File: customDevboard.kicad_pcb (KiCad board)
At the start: 4 copper layers, 87.7 x 87.7 mm, 245 parts, among them J10 Debug, J11 To FC, J12 TimePulse, J13 DRDY, J14 C+, J15 C-, J17 From BEC, J18 ESC Logic Power, J19 Flight Controller Power, J2 USB_C_Receptacle_USB2.0_14P, J20 From BEC, J3 From BEC, J4 From Battery, J5 U_FL-R-SMT-1_10_, J6 Debug, J7 To GPS, J8 BZ+, J9 COL, Q1 BC817, Q10 FDMS8350LET40, Q11 FDMS8350LET40, Q14 FDMS8350LET40, Q15 FDMS8350LET40, Q16 FDMS8350LET40, Q17 FDMS8350LET40, Q18 FDMS8350LET40, Q19 FDMS8350LET40, Q2 AO3401A, Q20 FDMS8350LET40, Q27 FDMS8350LET40, Q28 FDMS8350LET40, Q29 FDMS8350LET40, Q30 FDMS8350LET40, Q31 FDMS8350LET40, Q32 FDMS8350LET40, Q39 FDMS8350LET40, Q4 FDMS8350LET40, Q40 FDMS8350LET40, Q41 FDMS8350LET40, Q42 FDMS8350LET40, Q43 FDMS8350LET40, Q44 FDMS8350LET40, Q6 FDMS8350LET40, Q7 FDMS8350LET40, U1 DPS310, U10 INA181, U11 NEO-M8N, U12 TLV75733PDBV, U13 LIS3MDL, U14 FD6288Q, U15 FD6288Q, U16 FD6288Q, U17 STM32F303C8T6, U3 TPD2EUSB30, U4 TPS5430DDA, U5 STM32F722RET6, U6 TLV75733PDRV, U7 BMI270, U8 TLV75733PDBV, U9 FD6288Q, Y1 8MHz, Y2 32.768KHz, Y3 8 MHz

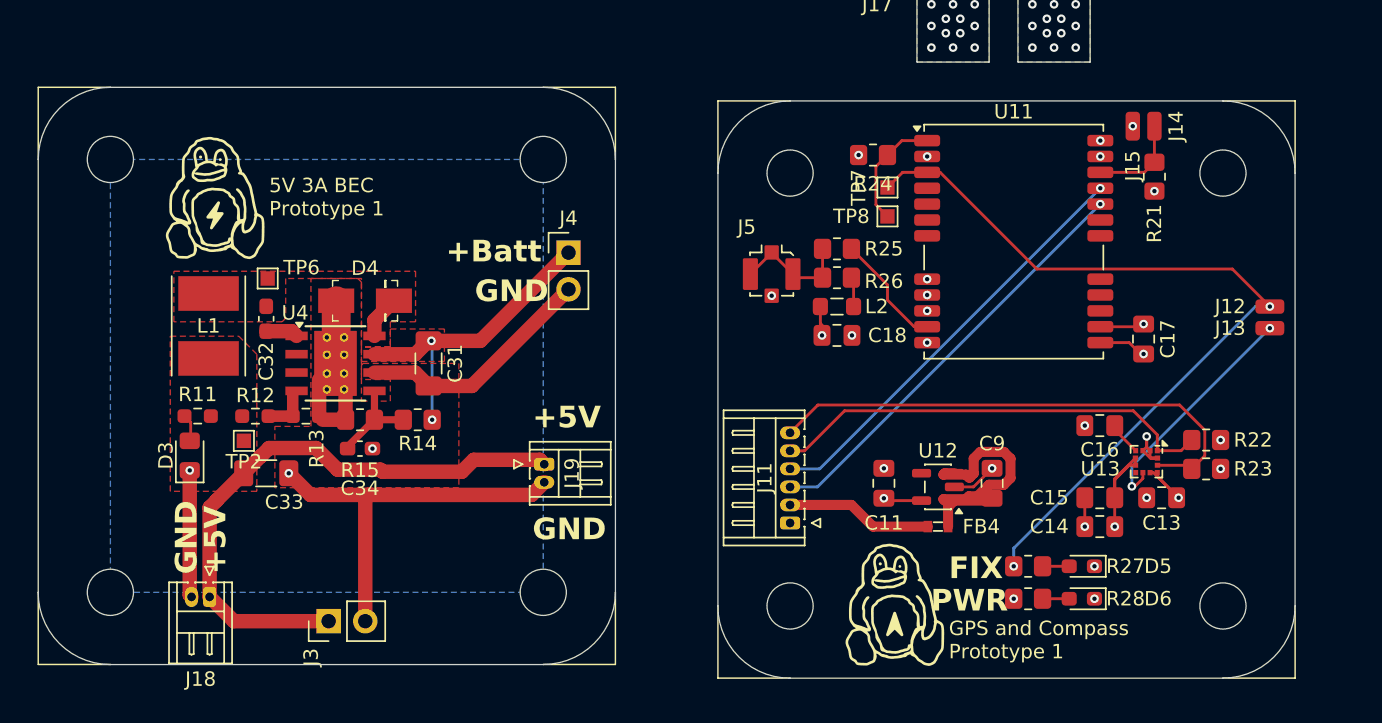
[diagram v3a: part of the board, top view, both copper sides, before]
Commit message: GPS has been moved to its own project
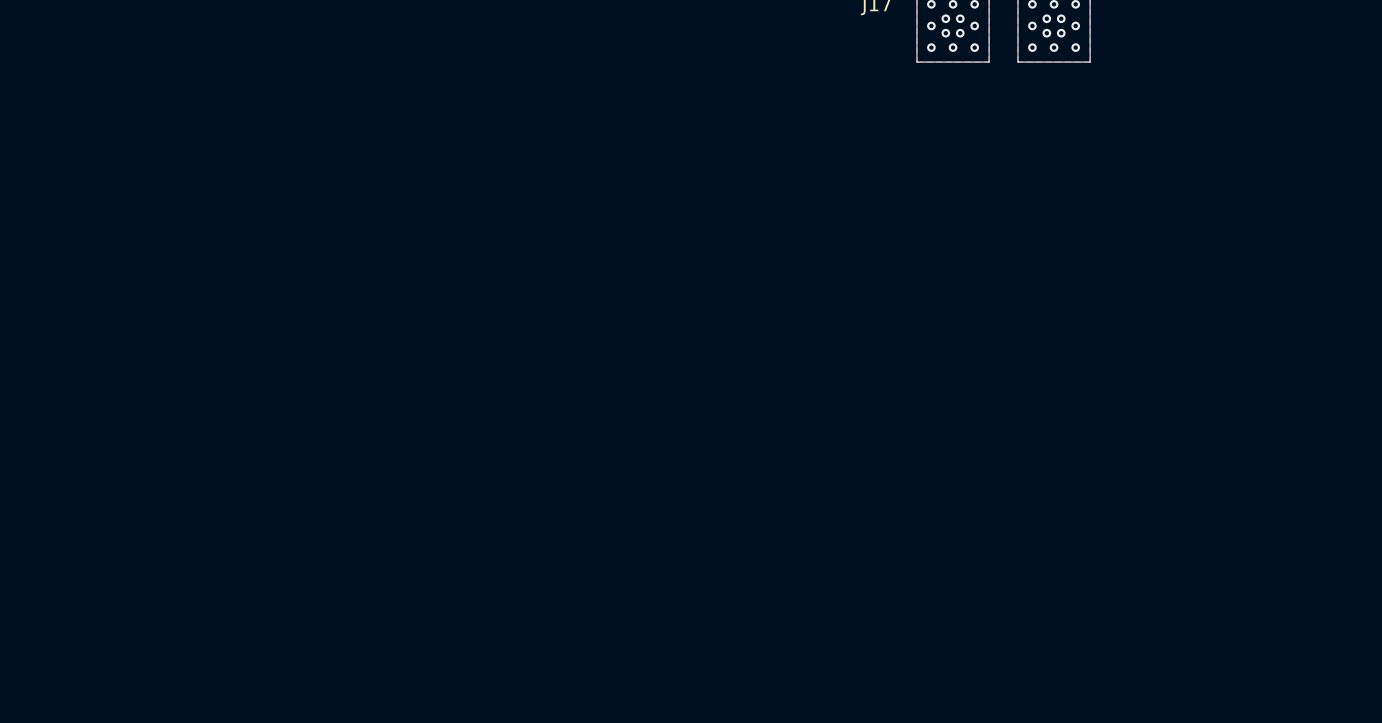
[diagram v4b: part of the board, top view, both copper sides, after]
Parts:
- removed C11, C14, C9: 1uF, Capacitor_SMD:C_0805_2012Metric_Pad1.18x1.45mm_HandSolder
- removed C13, C15, C17, C18: 100nF, Capacitor_SMD:C_0805_2012Metric_Pad1.18x1.45mm_HandSolder
- removed C16: 10nF, Capacitor_SMD:C_0805_2012Metric_Pad1.18x1.45mm_HandSolder
- removed C31: 10uF, Capacitor_SMD:C_1206_3216Metric_Pad1.33x1.80mm_HandSolder
- removed C32, C34: 10nF, Capacitor_SMD:C_0603_1608Metric_Pad1.08x0.95mm_HandSolder
- removed C33: 220uF, Capacitor_SMD:C_1206_3216Metric_Pad1.33x1.80mm_HandSolder
- removed D3: 5V LED, LED_SMD:LED_0805_2012Metric_Pad1.15x1.40mm_HandSolder
- removed D4: B340A, digikey-footprints:DO-214AC
- removed D5, D6: Status LED, LED_SMD:LED_0603_1608Metric_Pad1.05x0.95mm_HandSolder
- removed FB4: BLM18AG601SN1D, digikey-footprints:0603
- removed the G*** at (75.0, 98.2)
- removed the G*** at (27.9, 70.0)
- removed J11: To FC, Connector_Hirose:Hirose_DF13-06P-1.25DS_1x06_P1.25mm_Horizontal
- removed J12: TimePulse, Connector_Wire:SolderWirePad_1x01_SMD_1x2mm
- removed J13: DRDY, Connector_Wire:SolderWirePad_1x01_SMD_1x2mm
- removed J14: C+, Connector_Wire:SolderWirePad_1x01_SMD_1x2mm
- removed J15: C-, Connector_Wire:SolderWirePad_1x01_SMD_1x2mm
- removed J18: ESC Logic Power, Connector_Hirose:Hirose_DF13-02P-1.25DS_1x02_P1.25mm_Horizontal
- removed J19: Flight Controller Power, Connector_Hirose:Hirose_DF13-02P-1.25DS_1x02_P1.25mm_Horizontal
- removed J3: From BEC, Connector_PinHeader_2.54mm:PinHeader_1x02_P2.54mm_Vertical
- removed J4: From Battery, Connector_PinHeader_2.54mm:PinHeader_1x02_P2.54mm_Vertical
- removed J5: U_FL-R-SMT-1_10_, Connector_Coaxial:U.FL_Molex_MCRF_73412-0110_Vertical
- removed L1: 18uH, Inductor_SMD:L_Taiyo-Yuden_NR-50xx_HandSoldering
- removed L2: 10nH, Inductor_SMD:L_0805_2012Metric_Pad1.05x1.20mm_HandSolder
- removed R11: 10K, Resistor_SMD:R_0603_1608Metric_Pad0.98x0.95mm_HandSolder
- removed R12: 10k, Resistor_SMD:R_0603_1608Metric_Pad0.98x0.95mm_HandSolder
- removed R13: 3.24k, Resistor_SMD:R_0603_1608Metric_Pad0.98x0.95mm_HandSolder
- removed R14: 100k, Resistor_SMD:R_0805_2012Metric_Pad1.20x1.40mm_HandSolder
- removed R15: 18k, Resistor_SMD:R_0805_2012Metric_Pad1.20x1.40mm_HandSolder
- removed R21: 100, Resistor_SMD:R_0805_2012Metric_Pad1.20x1.40mm_HandSolder
- removed R22, R23: 47, Resistor_SMD:R_0805_2012Metric_Pad1.20x1.40mm_HandSolder
- removed R24: 10k, Resistor_SMD:R_0805_2012Metric_Pad1.20x1.40mm_HandSolder
- removed R25, R26: 0, Resistor_SMD:R_0805_2012Metric_Pad1.20x1.40mm_HandSolder
- removed R27, R28: 1K, Resistor_SMD:R_0805_2012Metric_Pad1.20x1.40mm_HandSolder
- removed the REF** at (98.0, 67.9)
- removed the REF** at (68.0, 97.9)
- removed the REF** at (20.9, 97.0)
- removed the REF** at (50.9, 67.0)
- removed the REF** at (68.0, 67.9)
- removed the REF** at (98.0, 97.9)
- removed the REF** at (20.9, 67.0)
- removed the REF** at (50.9, 97.0)
- removed TP2: +5V, TestPoint:TestPoint_Pad_1.0x1.0mm
- removed TP6: Per datasheet, TestPoint:TestPoint_Pad_1.0x1.0mm
- removed TP7: TimePulse, TestPoint:TestPoint_Pad_1.0x1.0mm
- removed TP8: SAFEBOOT, TestPoint:TestPoint_Pad_1.0x1.0mm
- removed U11: NEO-M8N, RF_GPS:ublox_NEO
- removed U12: TLV75733PDBV, Package_TO_SOT_SMD:SOT-23-5
- removed U13: LIS3MDL, Package_LGA:LGA-12_2x2mm_P0.5mm
- removed U4: TPS5430DDA, Package_SO:TI_SO-PowerPAD-8_ThermalVias
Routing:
- net BEC_GND: track 67.5 -> 0.00 mm, vias 3 -> 0
- net TimePulse: track 56.7 -> 0.00 mm, vias 2 -> 0
- net BEC_OUT: track 41.2 -> 0.00 mm
- net GPS_SDA: track 35.8 -> 0.00 mm
- net GPS_SCL: track 31.1 -> 0.00 mm
- net GPS_TX: track 29.6 -> 0.00 mm, vias 1 -> 0
- net GPS_RX: track 29.6 -> 0.00 mm, vias 1 -> 0
- net BEC_VIN: track 21.9 -> 0.00 mm, vias 2 -> 0
- net GPS_3.3V: track 21.8 -> 0.00 mm, vias 13 -> 0
- net Net-(U12-EN): track 19.1 -> 0.00 mm
- net DRDY: track 16.3 -> 0.00 mm, vias 2 -> 0
- net GPS_GND: track 12.9 -> 0.00 mm, vias 16 -> 0
- net GPS_5V: track 10.2 -> 0.00 mm
- net Net-(J5-Pad2): track 8.35 -> 0.00 mm
- net Net-(U11-~{SAFEBOOT}): track 8.33 -> 0.00 mm
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- removed copper zone on B.Cu, net BEC_GND
- removed copper zone on F.Cu, net BEC_GND
- removed copper zone on F.Cu, net BEC_OUT
- removed copper zone on F.Cu, net BEC_VIN
- removed copper zone on In1.Cu, net GPS_3.3V
- removed copper zone on In2.Cu, net GPS_GND
- removed copper zone on F.Cu, net Net-(U4-PH)
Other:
- board size 87.7 x 87.7 mm -> 87.5 x 45 mm
- board text removed: "+Batt"
- board text removed: "5V 3A BEC Prototype 1"
- board text removed: "FIX"
- board text removed: "GPS and Compass Prototype 1"
- board text removed: "PWR"

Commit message: ready for production almost
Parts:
- removed C12, C45, C50, C55: 10uF, Capacitor_SMD:C_0805_2012Metric_Pad1.18x1.45mm_HandSolder
- removed C35, C42, C43, C46, C51, C56, C60, C61, C62, C63, C65, C66: 100nF, Capacitor_SMD:C_0805_2012Metric_Pad1.18x1.45mm_HandSolder
- removed C37, C38, C39, C47, C48, C49, C52, C53, C54, C57, C58, C59: 220nF, Capacitor_SMD:C_0805_2012Metric_Pad1.18x1.45mm_HandSolder
- removed C40: 1uF, Capacitor_SMD:C_0603_1608Metric_Pad1.08x0.95mm_HandSolder
- removed C41: 2.2uF, Capacitor_SMD:C_0603_1608Metric_Pad1.08x0.95mm_HandSolder
- removed C44, C64: 1uF, Capacitor_SMD:C_0805_2012Metric_Pad1.18x1.45mm_HandSolder
- removed D10, D12, D13, D14, D15, D16, D17, D18, D19, D20, D7, D9: BAS21, Package_TO_SOT_SMD:SOT-23
- removed D11, D21: 3.3V LED, LED_SMD:LED_0402_1005Metric
- removed D8: SM6T22A, Diode_SMD:D_SMB
- removed the G*** at (82.8, 35.3)
- removed Q10, Q11, Q14, Q15, Q16, Q17, Q18, Q19, Q20, Q27, Q28, Q29, Q30, Q31, Q32, Q39, Q4, Q40, Q41, Q42, Q43, Q44, Q6, Q7: FDMS8350LET40, Package_TO_SOT_SMD:TDSON-8-1
- removed R29: 0.5m, Resistor_SMD:R_Shunt_Ohmite_LVK12
- removed R32, R33, R34, R35, R38, R39, R47, R48, R49, R50, R51, R52, R60, R61, R62, R63, R64, R65, R72, R73, R74, R75, R76, R77: 10, Resistor_SMD:R_0805_2012Metric_Pad1.20x1.40mm_HandSolder
- removed R42: 100k, Resistor_SMD:R_0603_1608Metric_Pad0.98x0.95mm_HandSolder
- removed R43, R84: 10K, Resistor_SMD:R_0603_1608Metric_Pad0.98x0.95mm_HandSolder
- removed R44: 50k, Resistor_SMD:R_0603_1608Metric_Pad0.98x0.95mm_HandSolder
- removed R45, R46, R59: 10k, Resistor_SMD:R_0603_1608Metric_Pad0.98x0.95mm_HandSolder
- removed the REF** at (67.8, 50.2)
- removed the REF** at (97.8, 50.2)
- removed the REF** at (67.8, 20.2)
- removed the REF** at (97.8, 20.2)
- removed TP9: +3.3V, TestPoint:TestPoint_Pad_1.0x1.0mm
- removed U10: INA181, Package_TO_SOT_SMD:SOT-23-6
- removed U14, U15, U16, U9: FD6288Q, FD6288Q:QFN50P400X400X90-25N
- removed U17: STM32F303C8T6, Package_QFP:LQFP-48_7x7mm_P0.5mm
- removed U8: TLV75733PDBV, Package_TO_SOT_SMD:SOT-23-5
- removed Y3: 8 MHz, Crystal:Resonator_SMD_Murata_CSTxExxV-3Pin_3.0x1.1mm
- added J1: Conn_01x01, Connector_Wire:SolderWirePad_1x01_SMD_1x2mm, F.Cu at (24.5, 17.8)
- added J11: Conn_01x01, Connector_Wire:SolderWirePad_1x01_SMD_1x2mm, F.Cu at (42.8, 17.8)
- added J12: Conn_01x01, Connector_Wire:SolderWirePad_1x01_SMD_1x2mm, F.Cu at (44.2, 17.8)
- added J13: Conn_01x01, Connector_Wire:SolderWirePad_1x01_SMD_1x2mm, F.Cu at (45.8, 17.8)
- added J14: Conn_01x01, Connector_Wire:SolderWirePad_1x01_SMD_1x2mm, F.Cu at (40.5, 52.8)
- added J15: Conn_01x01, Connector_Wire:SolderWirePad_1x01_SMD_1x2mm, F.Cu at (39.0, 52.8)
- added J16: Conn_01x01, Connector_Wire:SolderWirePad_1x01_SMD_1x2mm, F.Cu at (37.5, 52.8)
- added J18: Conn_01x01, Connector_Wire:SolderWirePad_1x01_SMD_1x2mm, F.Cu at (34.5, 52.8)
- added J19: Conn_01x01, Connector_Wire:SolderWirePad_1x01_SMD_1x2mm, F.Cu at (33.0, 52.8)
- added J21: Conn_01x01, Connector_Wire:SolderWirePad_1x01_SMD_1x2mm, F.Cu at (31.5, 52.8)
- added J22: Conn_01x01, Connector_Wire:SolderWirePad_1x01_SMD_1x2mm, F.Cu at (30.0, 52.8)
- added J23: Conn_01x01, Connector_Wire:SolderWirePad_1x01_SMD_1x2mm, F.Cu at (16.8, 31.0)
- added J24: Conn_01x01, Connector_Wire:SolderWirePad_1x01_SMD_1x2mm, F.Cu at (16.8, 32.5)
- added J25: Conn_01x01, Connector_Wire:SolderWirePad_1x01_SMD_1x2mm, F.Cu at (16.8, 34.0)
- added J26: Conn_01x01, Connector_Wire:SolderWirePad_1x01_SMD_1x2mm, F.Cu at (16.8, 35.5)
- added J27: Conn_01x01, Connector_Wire:SolderWirePad_1x01_SMD_1x2mm, F.Cu at (24.2, 53.2)
- added J3: Conn_01x01, Connector_Wire:SolderWirePad_1x01_SMD_1x2mm, F.Cu at (26.1, 17.8)
- added J4: Conn_01x01, Connector_Wire:SolderWirePad_1x01_SMD_1x2mm, F.Cu at (27.6, 17.8)
- added J5: Conn_01x01, Connector_Wire:SolderWirePad_1x01_SMD_1x2mm, F.Cu at (29.1, 17.8)
- J10: value Debug -> Conn_01x01
- J17: value From BEC -> Conn_01x01; footprint Connector_Hirose:Hirose_DF13-02P-1.25DS_1x02_P1.25mm_Horizontal -> Connector_Wire:SolderWirePad_1x01_SMD_1x2mm
- moved J17 38.7 mm to (36.0, 52.8)
- moved J10 35.6 mm to (41.2, 17.8), turned to 0 degrees
- moved J9 5.01 mm to (44.5, 52.8)
- moved J8 4.02 mm to (46.0, 52.8)
- moved C3 0.44 mm to (29.5, 44.5)
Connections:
- J10 pad 1: ESC_SYS_JTMS-SWDIO -> PB3
- J17 pad 1: ESC_5V -> PC7
- U5 pad 11: unconnected-(U5-PC3-Pad11) -> PC3
- U5 pad 14: unconnected-(U5-PA0-Pad14) -> PA0
- U5 pad 15: unconnected-(U5-PA1-Pad15) -> PA1
- U5 pad 27: unconnected-(U5-PB2-Pad27) -> PB2
- U5 pad 33: unconnected-(U5-PB12-Pad33) -> PB12
- U5 pad 35: unconnected-(U5-PB14-Pad35) -> PB14
- U5 pad 36: unconnected-(U5-PB15-Pad36) -> PB15
- U5 pad 37: unconnected-(U5-PC6-Pad37) -> PC6
- U5 pad 38: unconnected-(U5-PC7-Pad38) -> PC7
- U5 pad 39: unconnected-(U5-PC8-Pad39) -> PC8
- U5 pad 40: unconnected-(U5-PC9-Pad40) -> PC9
- U5 pad 41: unconnected-(U5-PA8-Pad41) -> PA8
- U5 pad 50: unconnected-(U5-PA15-Pad50) -> PA15
- U5 pad 53: unconnected-(U5-PC12-Pad53) -> PC12
- U5 pad 54: unconnected-(U5-PD2-Pad54) -> PD2
- U5 pad 55: unconnected-(U5-PB3-Pad55) -> PB3
- U5 pad 56: unconnected-(U5-PB4-Pad56) -> PB4
- U5 pad 57: unconnected-(U5-PB5-Pad57) -> PB5
- U5 pad 61: unconnected-(U5-PB8-Pad61) -> PB8
- U5 pad 62: unconnected-(U5-PB9-Pad62) -> PB9
- U5 pad 8: unconnected-(U5-PC0-Pad8) -> PC0
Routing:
- net GND: track 37.0 -> 63.9 mm, vias 26 -> 29
- net PB14: track 0.00 -> 23.9 mm
- net PB12: track 0.00 -> 22.8 mm
- net PC7: track 0.00 -> 22.3 mm
- net PC6: track 0.00 -> 22.1 mm
- net PC8: track 0.00 -> 21.9 mm
- net PA1: track 0.00 -> 21.9 mm, vias 0 -> 2
- net PC9: track 0.00 -> 21.8 mm
- net PB15: track 0.00 -> 21.5 mm
- net PA8: track 0.00 -> 21.3 mm
- net ESC_M1_PHASE_3_HIGH: track 21.3 -> 0.00 mm, vias 1 -> 0
- net PB9: track 0.00 -> 20.6 mm, vias 0 -> 2
- net PC0: track 0.00 -> 20.5 mm, vias 0 -> 2
- net PA0: track 0.00 -> 20.3 mm
- net PB2: track 0.00 -> 20.1 mm
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- removed copper zone on B.Cu, net ESC_COM
- removed copper zone on F.Cu, net ESC_COM
- removed copper zone on F.Cu, net ESC_UNSAFE_VBAT+
- removed copper zone on F.Cu, net ESC_UNSAFE_VBAT-
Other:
- board size 87.5 x 45 mm -> 40 x 40 mm
- board text added: "FC P1"
- board text removed: "ESC Prototype 1"
- board text removed: "Flight Controller Prototype 1"
- board text removed: "V+"
- board text removed: "V-"

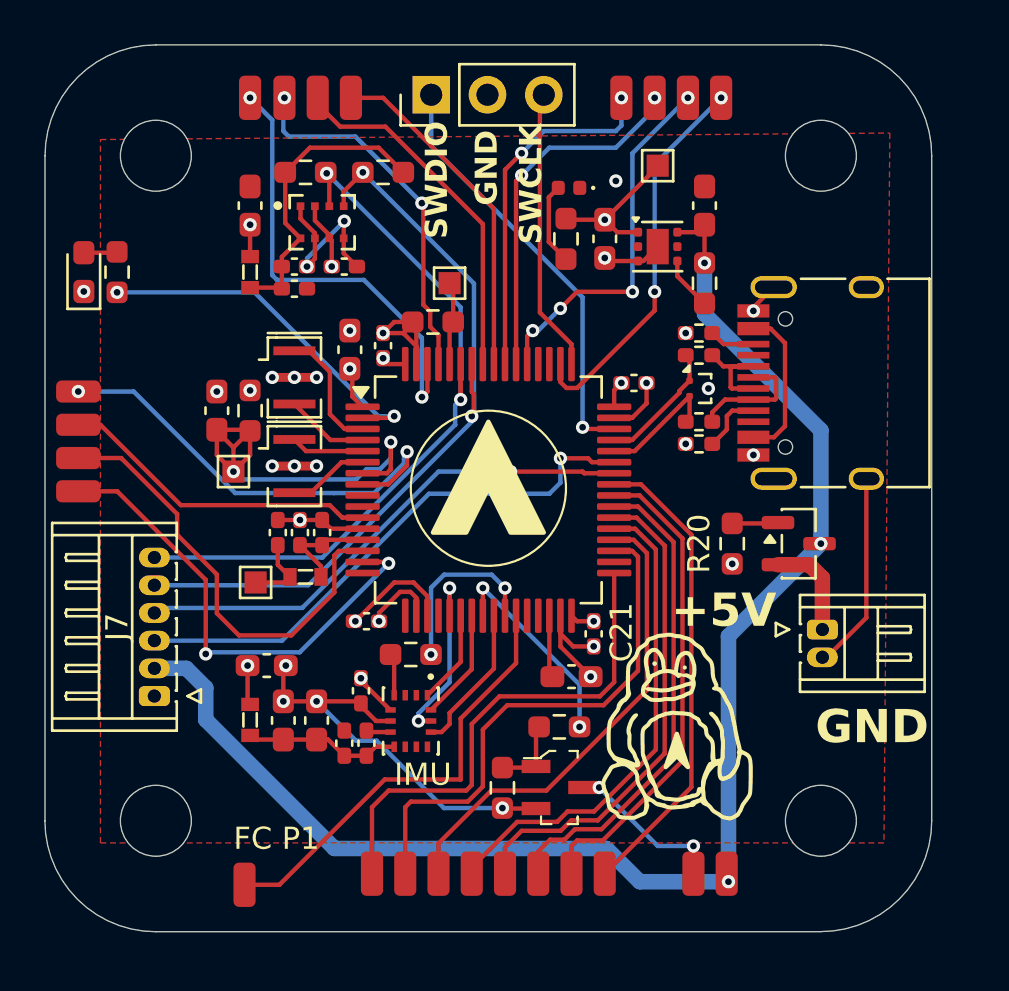
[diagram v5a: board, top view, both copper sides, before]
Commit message: fix drc issues and blender render
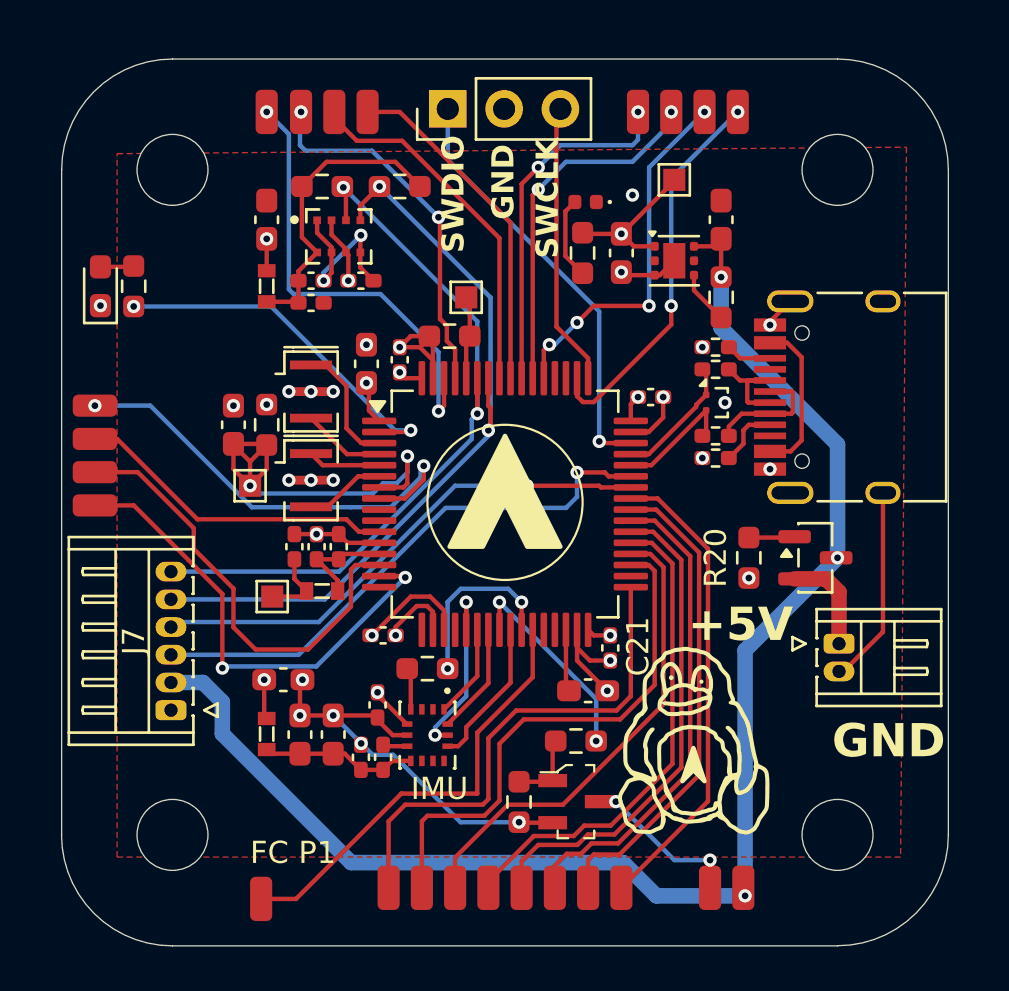
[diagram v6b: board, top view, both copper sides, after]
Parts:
- removed REF** (x4): MountingHole_3.2mm_M3, MountingHole:MountingHole_3.2mm_M3
- added H1: MountingHole, MountingHole:MountingHole_3.2mm_M3, F.Cu at (21.0, 21.0)
- added H2: MountingHole, MountingHole:MountingHole_3.2mm_M3, F.Cu at (51.0, 21.0)
- added H3: MountingHole, MountingHole:MountingHole_3.2mm_M3, F.Cu at (51.0, 51.0)
- added H4: MountingHole, MountingHole:MountingHole_3.2mm_M3, F.Cu at (21.0, 51.0)
- moved C1 0.98 mm to (29.5, 47.5)
- moved C10 0.98 mm to (26.8, 46.5)
- moved C2 0.98 mm to (30.5, 47.5)
- moved C21 0.98 mm to (40.8, 42.6)
- moved C22 0.98 mm to (30.5, 42.0)
- moved C24 0.98 mm to (27.5, 38.0)
- moved C25 0.98 mm to (28.5, 38.0)
- moved C26 0.98 mm to (26.5, 38.0)
- moved C27 0.98 mm to (39.8, 44.5)
- moved C3 0.98 mm to (30.2, 45.1)
- moved C7 0.98 mm to (26.0, 44.0)
- moved C8 0.98 mm to (28.2, 46.5)
- moved FB1 0.98 mm to (27.8, 40.0)
- moved FB3 0.98 mm to (25.2, 46.5)
- moved J14 0.98 mm to (41.2, 53.4)
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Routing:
- net GND: vias 29 -> 30
